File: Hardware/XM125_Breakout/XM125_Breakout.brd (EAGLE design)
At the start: 50.8 x 50.8 mm, 57 parts, among them J2 QWIIC_RIGHT_ANGLE, J3 QWIIC_RIGHT_ANGLE, U1 XM125, U4 CH340C, U5 ESD Diode

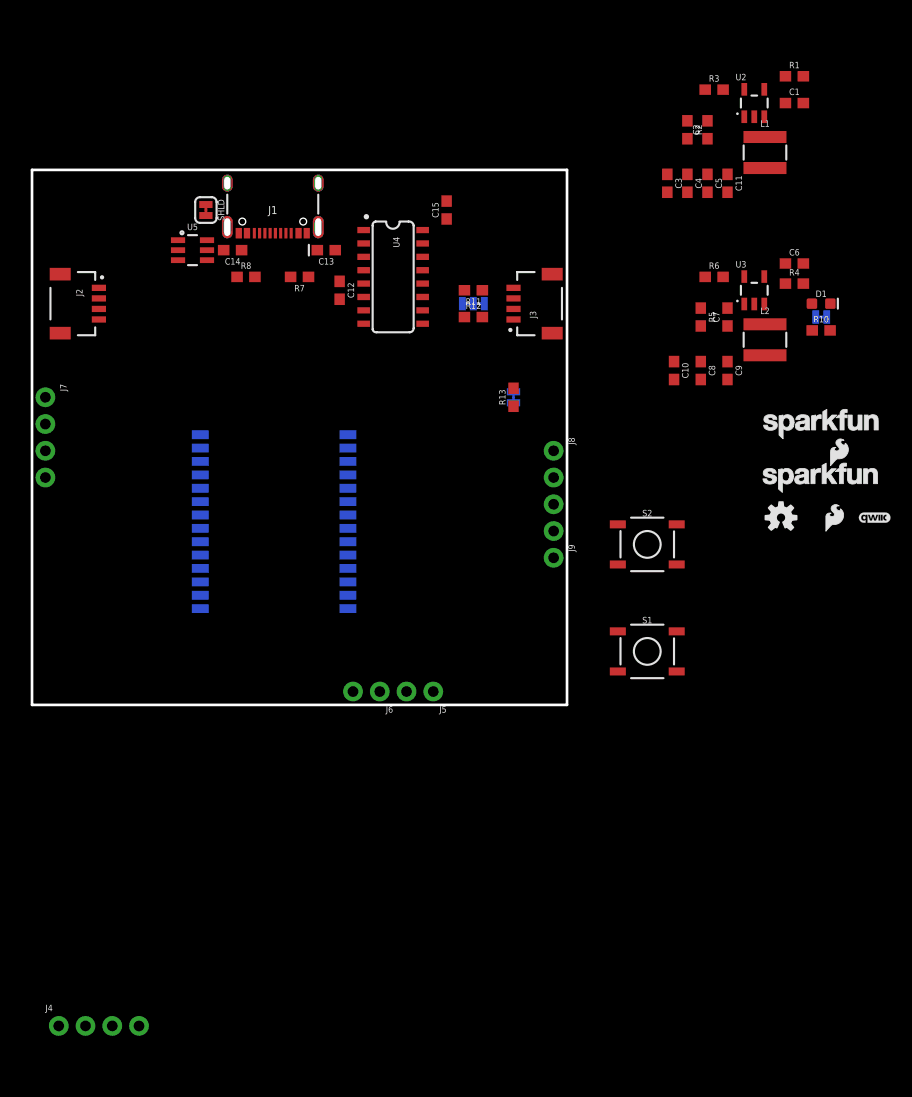
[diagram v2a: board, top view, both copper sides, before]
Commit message: Updates as per schematic review
For full detailed list of changes, see XM125 Schematic review document
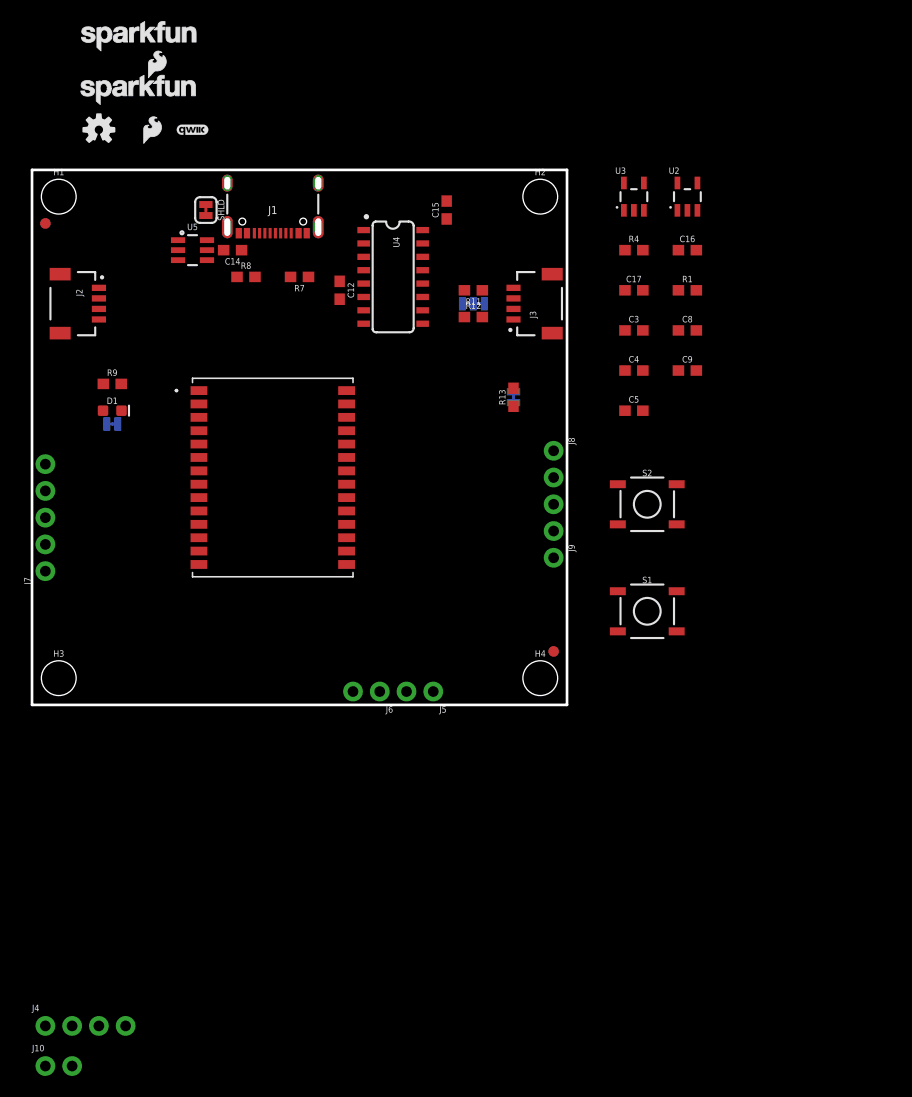
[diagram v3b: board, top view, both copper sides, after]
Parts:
- removed 3V3: JUMPER-SMT_2_NC_TRACE_SILK, SparkFun-Jumpers:SMT-JUMPER_2_NC_TRACE_SILK
- removed C1, C11, C2, C6: 22uF, SparkFun-Capacitors:0603
- removed C10: 1.0uF, SparkFun-Capacitors:0603
- removed C13: 10uF, SparkFun-Capacitors:0603-POLAR
- removed C7: 22pF, SparkFun-Capacitors:0603
- removed L1, L2: 2.2μH, SparkFun-Coils:INDUCTOR_4X4MM
- removed R10: 1k, SparkFun-Resistors:0603
- removed R2: 300k, SparkFun-Resistors:0603
- removed R3: 150k, SparkFun-Resistors:0603
- removed R5: 453k, SparkFun-Resistors:0603
- removed R6: 100k, SparkFun-Resistors:0603
- added C16, C17: 2.2uF, SparkFun-Capacitors:0603
- added FD1, FD2, FD3, FD4: FIDUCIAL1X2, SparkFun-Aesthetics:FIDUCIAL-1X2
- added H1, H2, H3, H4: STAND-OFF, SparkFun-Hardware:STAND-OFF
- added J10: (no value), SparkFun-Connectors:1X02_NO_SILK
- added PWR_LED: JUMPER-SMT_2_NC_TRACE_SILK, SparkFun-Jumpers:SMT-JUMPER_2_NC_TRACE_SILK
- added R9: 4.7k, SparkFun-Resistors:0603
- J7: device SparkFun-Connectors:1X04_NO_SILK -> SparkFun-Connectors:1X05_NO_SILK
- U2: value (none) -> RT9080-33GJ5
- U3: value (none) -> RT9080-18GJ5; device SparkFun-IC-Power:SOT23-5 -> XM125:SOT23-5
- moved LOGO2 74.5 mm to (15.2, 54.6)
- moved LOGO3 74.5 mm to (10.2, 58.4)
- moved LOGO4 74.5 mm to (6.35, 54.6)
- moved LOGO5 74.5 mm to (11.4, 54.6)
- moved LOGO6 74.5 mm to (10.2, 63.5)
- moved D1 68.1 mm to (7.62, 27.9)
- moved R1 22.7 mm to (62.2, 39.4)
- moved C5 22.7 mm to (57.1, 27.9), turned to 0 degrees
- moved C4 18.5 mm to (57.1, 31.8), turned to 0 degrees
- moved J7 16.5 mm to (1.27, 12.7), turned to 90 degrees
- moved R4 15.6 mm to (57.1, 43.2)
- moved U3 14.5 mm to (57.1, 48.3)
- moved C3 14.3 mm to (57.1, 35.6), turned to 0 degrees
- moved U2 10.9 mm to (62.2, 48.3)
- moved U1 4.19 mm to (22.9, 21.6), flipped to the top, turned to 0 degrees
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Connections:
- removed net INT: J4.1
- removed net N$3: L1.P$1, U2.3
- removed net N$4: R1.2, U2.1
- removed net N$5: R4.2, U3.1
- removed net N$6: C2.2, R2.1, R3.1, U2.5
- removed net N$7: L2.P$1, U3.3
- removed net N$8: C7.2, R5.1, R6.2, U3.5
- new net N$13: R1.2, U2.3
- new net N$20: R4.2, U3.3
- net 1.8V: now also J7.5, U3.5; no longer C11.1, C2.1, J7.4, L1.P$2, R2.2
- net 3.3V: now also J4.2, J7.4, PWR_LED.2, U2.5; no longer 3V3.2, C10.1, C7.1, J7.3, L2.P$2, R5.2, S1.3, S1.4, S2.3, S2.4
- net CH340-CTS: now also U1.9; no longer U1.8
- net CH340-RTS: now also U1.8; no longer U1.9
- net GND: now also C16.2, C17.2, J4.1, S1.3, S1.4, S2.3, S2.4; no longer C1.2, C10.2, C11.2, C13.-, C6.2, R3.2, R6.1
- net N$14: now also PWR_LED.1, R9.2; no longer 3V3.1, R10.2
- net N$15: now also R9.1; no longer R10.1
- net SCL: now also J4.4; no longer J4.3
- net SDA: now also J4.3; no longer J4.2
- net V_USB: now also C16.1, C17.1, J7.3, U2.1, U3.1; no longer C1.1, C13.+, C6.1, U2.4, U3.4
- net WAKE_UP: no longer S2.1, S2.2
- net XM125_GPIO2/BOOT0: now also S2.1, S2.2
- net XM125_I2C_ADDRESS: now also J10.2; no longer J4.4
- net XM125_INT: now also J10.1

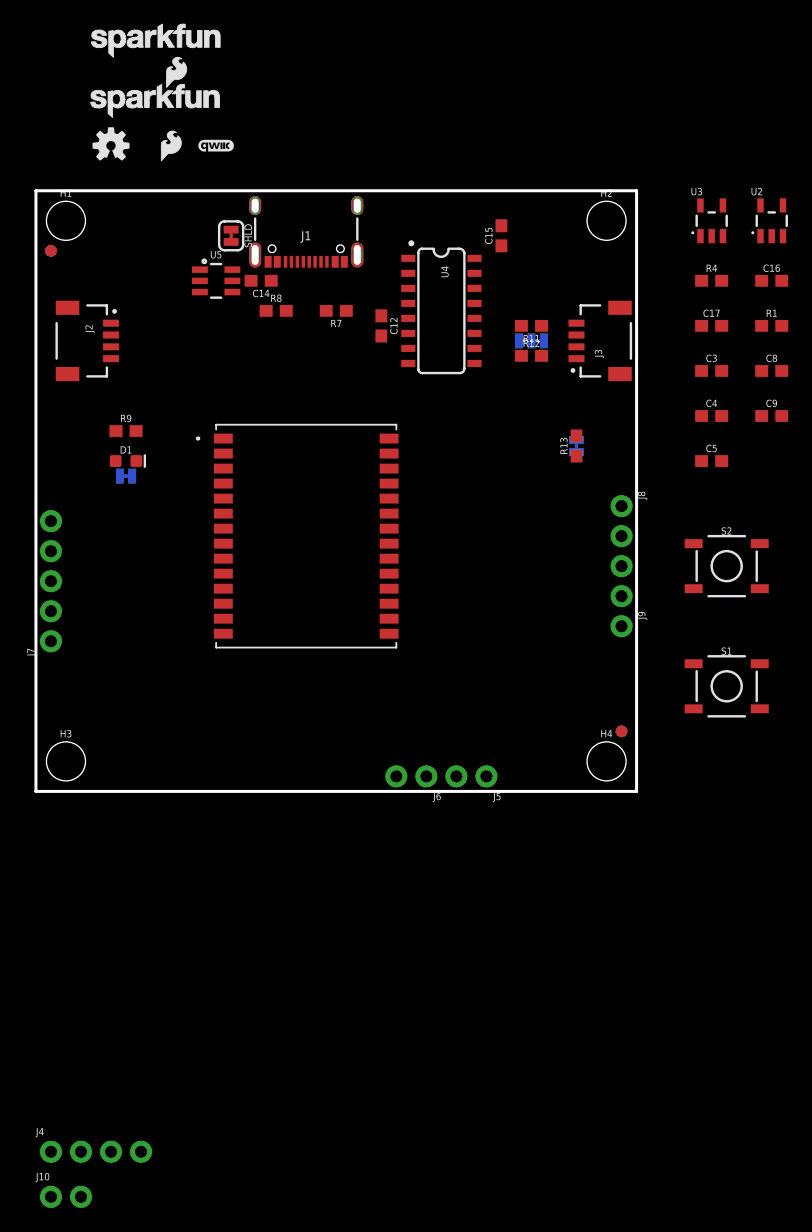
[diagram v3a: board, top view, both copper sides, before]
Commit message: Updated files for design review
Nearing completion and ready for design review - completed layout, added measures, added labels, name, logos
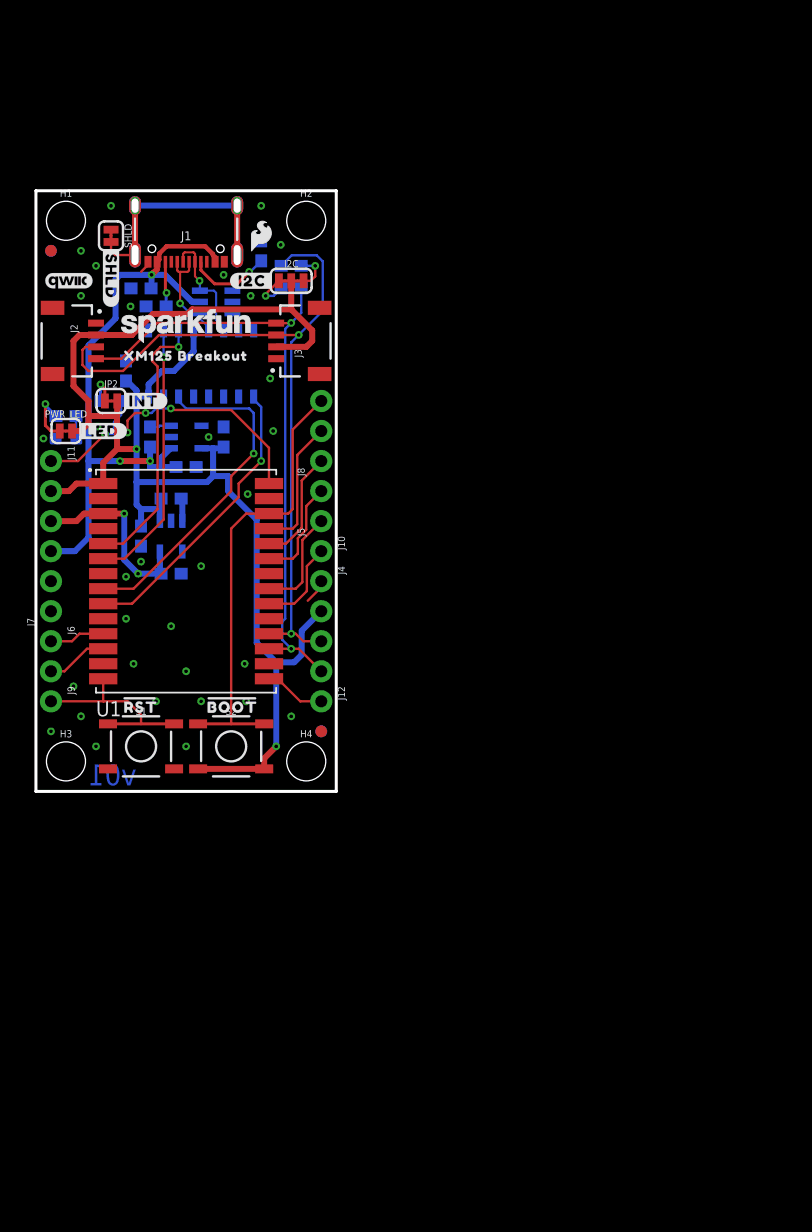
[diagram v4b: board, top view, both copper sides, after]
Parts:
- removed C12: 10nF, SparkFun-Capacitors:0603
- removed C4, C9: 0.1uF, SparkFun-Capacitors:0603
- removed C5: 1.0uF, SparkFun-Capacitors:0603
- added J11, J12: (no value), SparkFun-Connectors:1X01_NO_SILK_STAND
- added U$1, U$60: (no value), output:#GND#17
- added U$10: (no value), output:#SCL#8
- added U$11: (no value), output:BOOT21630063003532
- added U$12: (no value), output:PWR21630063003533
- added U$13: (no value), output:#SDA#9
- added U$14: (no value), output:#3V3#10
- added U$15: (no value), output:#GND#10
- added U$16: (no value), output:#3V3#18
- added U$17: (no value), output:#I2C_ADDR#11
- added U$18: (no value), output:#DEBUG_TX#0
- added U$19: (no value), output:#DEBUG_RX#3
- added U$2: (no value), output:#VUSB#5
- added U$20: (no value), output:#GPIO0#5
- added U$21: (no value), output:#GPIO1#5
- added U$22: (no value), output:#IO2#BOOT#5
- added U$24: (no value), output:XM125_BREAKOUT127
- added U$25: (no value), output:XM125_BREAKOUT0
- added U$26: (no value), output:#I2C#126
- added U$27: (no value), output:#LED#127
- added U$28: (no value), output:#INT#128
- added U$29: (no value), output:#SHLD#129
- added U$3: (no value), output:#INT#2
- added U$4: (no value), output:#1V8#3
- added U$5: (no value), output:RST1630063003525
- added U$6: (no value), output:#SWDIO#4
- added U$7: (no value), output:#CLK#5
- added U$8: (no value), output:#RESET#6
- added U$9: (no value), output:#WAKE_UP#7
- J10: device SparkFun-Connectors:1X02_NO_SILK -> SparkFun-Connectors:1X01_NO_SILK_STAND
- J8: device SparkFun-Connectors:1X04_NO_SILK -> SparkFun-Connectors:1X03_NO_SILK
- LOGO2: value QWIIC_LOGO_3MM -> QWIIC_LOGO_4MM; device SparkFun-Aesthetics:QWIIC_3MM -> SparkFun-Aesthetics:QWIIC_4MM
- moved LOGO1 89.8 mm to (54.6, 52.1)
- moved J10 59.2 mm to (24.1, 20.3), turned to 270 degrees
- moved R1 53.4 mm to (9.65, 30.0), flipped to the bottom, turned to 90 degrees
- moved J4 53.4 mm to (24.1, 17.8), turned to 270 degrees
- moved U3 52.9 mm to (11.4, 21.6), flipped to the bottom, turned to 180 degrees
- moved U2 52.8 mm to (12.7, 30.0), flipped to the bottom, turned to 90 degrees
- moved C16 52.0 mm to (12.7, 27.4), flipped to the bottom, turned to 180 degrees
- moved C17 51.4 mm to (8.89, 21.6), flipped to the bottom, turned to 270 degrees
- moved S1 49.8 mm to (8.89, 3.81)
- moved R4 49.3 mm to (11.4, 24.8), flipped to the bottom, turned to 180 degrees
- moved C3 48.8 mm to (11.4, 18.4), flipped to the bottom, turned to 180 degrees
- moved J9 48.7 mm to (1.27, 7.62)
- moved C8 46.7 mm to (15.9, 30.0), flipped to the bottom, turned to 90 degrees
- moved LOGO4 44.9 mm to (12.7, 10.2), flipped to the bottom
- moved S2 44.6 mm to (16.5, 3.81)
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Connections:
- removed net N$12: C12.1, U4.4
- net 1.8V: now also J7.4; no longer C4.1, C5.1, J7.5
- net 3.3V: now also C17.1, J7.5, R4.1, S2.3, S2.4, U3.1, U4.4; no longer C9.1, J7.4
- net GND: no longer C12.2, C4.2, C5.2, C9.2, R11.1, R12.1, S2.3, S2.4
- net SCL: now also R12.1
- net SDA: now also R11.1
- net V_USB: no longer C17.1, R4.1, U3.1
- net WAKE_UP: now also J12.1
- net XM125_I2C_ADDRESS: now also J10.1; no longer J10.2
- net XM125_INT: now also J11.1; no longer J10.1, J8.4
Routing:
- net 3.3V: track 0.00 -> 130.6 mm, vias 0 -> 2
- net SDA: track 0.00 -> 63.7 mm, vias 0 -> 2
- net V_USB: track 0.00 -> 54.7 mm, vias 0 -> 3
- net SCL: track 0.00 -> 54.5 mm, vias 0 -> 2
- net XM125_GPIO2/BOOT0: track 0.00 -> 38.1 mm
- net CH340-RTS: track 0.00 -> 28.8 mm, vias 0 -> 1
- net XM125_INT: track 0.00 -> 28.3 mm, vias 0 -> 4
- net CH340-CTS: track 0.00 -> 24.7 mm, vias 0 -> 1
- net CH340-RX: track 0.00 -> 22.9 mm, vias 0 -> 1
- net CH340-TX: track 0.00 -> 22.5 mm, vias 0 -> 1
- net N$9: track 0.00 -> 19.9 mm
- net XM125_RESET: track 0.00 -> 16.4 mm
- net 1.8V: track 0.00 -> 15.9 mm, vias 0 -> 2
- net XM125_GPIO1: track 0.00 -> 11.3 mm
- net N$2: track 0.00 -> 9.97 mm, vias 0 -> 1
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- added copper zone on layer 1, net GND
- added copper zone on layer 16, net GND
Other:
- board size 50.8 x 50.8 mm -> 25.4 x 50.8 mm
- board text added: "Solder Mask: Black Thickness: 1.6mm Two layer design Finish: HASL Lead-Free Copper Weight: 1oz Material: TG135-140"
- board text added: "v01"

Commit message: Slight aesthetic change - ready for review!
Ready for protos review
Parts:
- removed U$22: (no value), output:#IO2#BOOT#5
- added U$23: (no value), output:#IO2##BOOT#134
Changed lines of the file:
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@@
 <element name="U$20" library="output" package="#GPIO0#5" value="" x="20.701" y="27.94" smashed="yes" rot="MR0"/>
 <element name="U$21" library="output" package="#GPIO1#5" value="" x="20.828" y="30.226" smashed="yes" rot="MR0"/>
-<element name="U$22" library="output" package="#IO2#BOOT#5" value="" x="19.05" y="32.131" smashed="yes" rot="MR0"/>
 <element name="U$2" library="output" package="#VUSB#5" value="" x="4.445" y="20.32" smashed="yes" rot="MR0"/>
 <element name="U$24" library="output" package="XM125_BREAKOUT127" value="" x="12.7" y="36.83" smashed="yes"/>
@@
 <element name="U$28" library="output" package="#INT#128" value="" x="9.144" y="33.02" smashed="yes"/>
 <element name="U$29" library="output" package="#SHLD#129" value="" x="6.35" y="43.561" smashed="yes" rot="R270"/>
+<element name="U$23" library="output" package="#IO2##BOOT#134" value="" x="19.05" y="32.131" smashed="yes" rot="MR0"/>
 </elements>
 <signals>
